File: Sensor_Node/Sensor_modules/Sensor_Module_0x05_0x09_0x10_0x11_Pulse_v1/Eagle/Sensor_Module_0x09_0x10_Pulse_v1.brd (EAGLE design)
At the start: 55 x 35 mm, 21 parts, among them U2 ATMEGA328P_TQFP, Y1 8MHZ

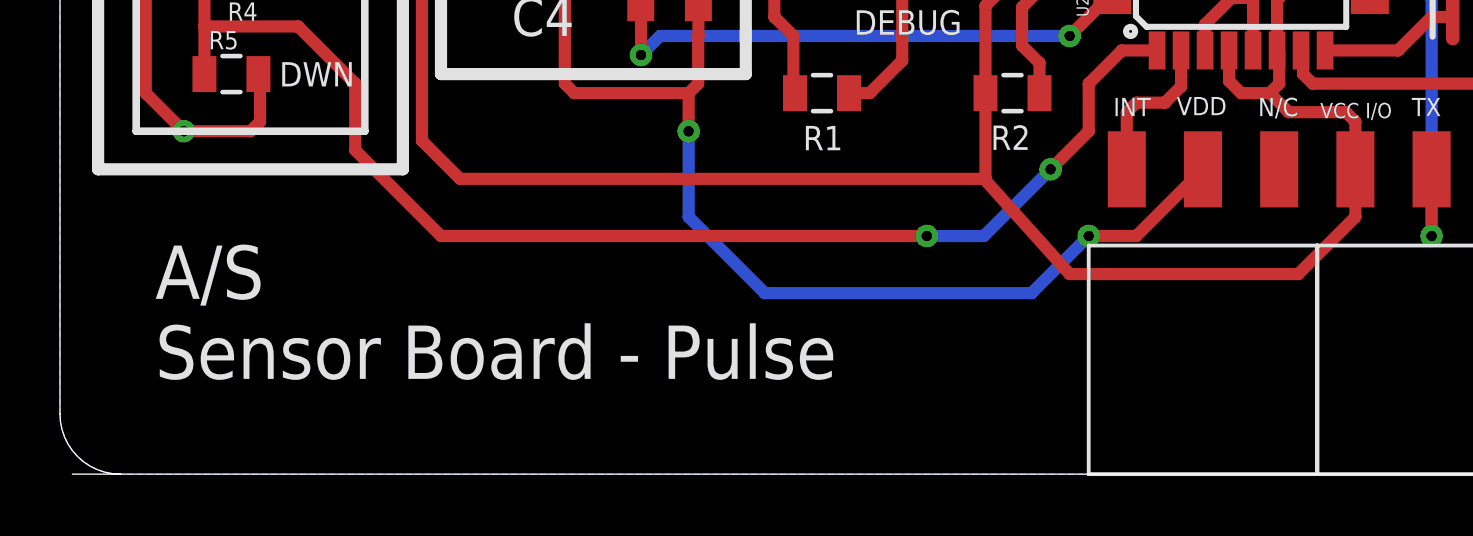
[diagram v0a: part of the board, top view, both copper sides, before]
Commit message: Renaming boards to modules inside eagle files
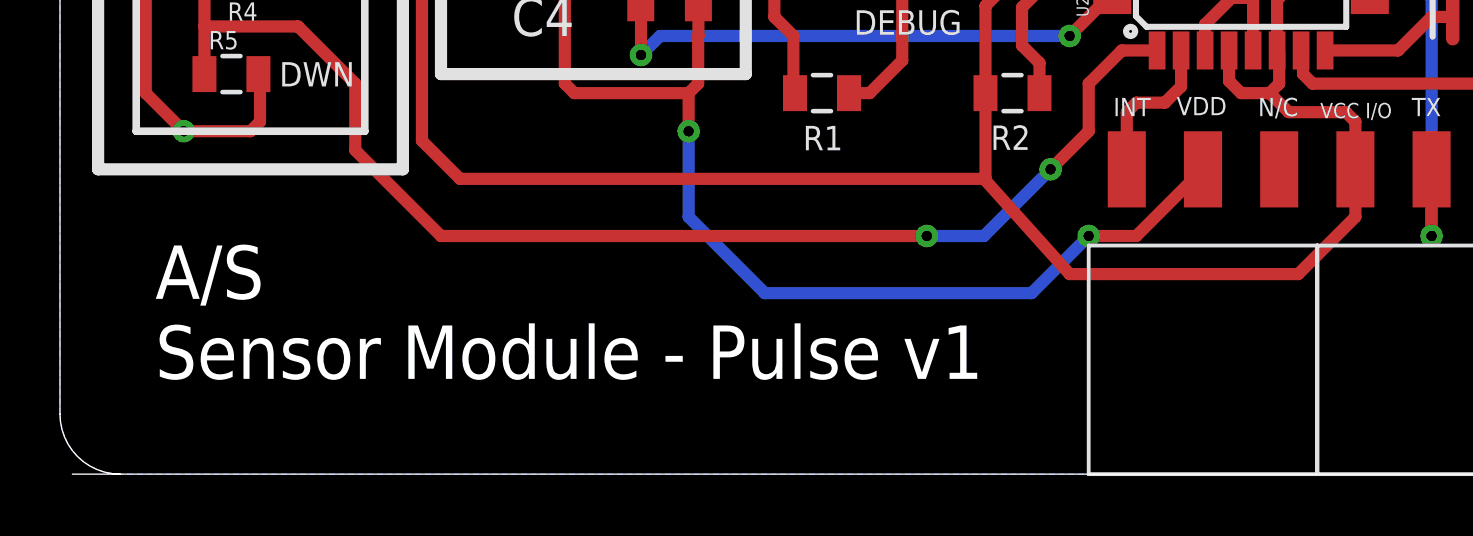
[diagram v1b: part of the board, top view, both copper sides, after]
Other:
- board text added: "A/S Sensor Module - Pulse v1"
- board text removed: "A/S Sensor Board - Pulse"
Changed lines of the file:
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@@
 <?xml version="1.0" encoding="utf-8"?>
 <!DOCTYPE eagle SYSTEM "eagle.dtd">
-<eagle version="8.4.1">
+<eagle version="9.1.1">
 <drawing>
 <settings>
@@
 <text x="4.7625" y="31.75" size="1.27" layer="21">DI 2</text>
 <text x="16.51" y="31.75" size="1.27" layer="21">DI 1</text>
-<text x="3.175" y="3.175" size="1.778" layer="21">A/S
-Sensor Board - Pulse</text>
+<text x="3.175" y="3.175" size="1.778" layer="20">A/S
+Sensor Module - Pulse v1</text>
 <hole x="9.525" y="30.48" drill="2.54"/>
 <hole x="3.175" y="30.48" drill="2.54"/>
@@
 <param name="checkRestrict" value="1"/>
 <param name="checkStop" value="0"/>
+<param name="checkValues" value="0"/>
+<param name="checkNames" value="1"/>
+<param name="checkWireStubs" value="1"/>
+<param name="checkPolygonWidth" value="0"/>
 <param name="useDiameter" value="13"/>
 <param name="maxErrors" value="50"/>
@@
 </signal>
 </signals>
+<mfgpreviewcolors>
+<mfgpreviewcolor name="soldermaskcolor" color="0xC8008000"/>
+<mfgpreviewcolor name="silkscreencolor" color="0xFFFEFEFE"/>
+<mfgpreviewcolor name="backgroundcolor" color="0xFF282828"/>
+<mfgpreviewcolor name="coppercolor" color="0xFFFFBF00"/>
+<mfgpreviewcolor name="substratecolor" color="0xFF786E46"/>
+</mfgpreviewcolors>
 </board>
 </drawing>
